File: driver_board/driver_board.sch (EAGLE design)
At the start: 18 parts, among them Q1 IRLML6346TRPBF, U1 AL5812MP-13

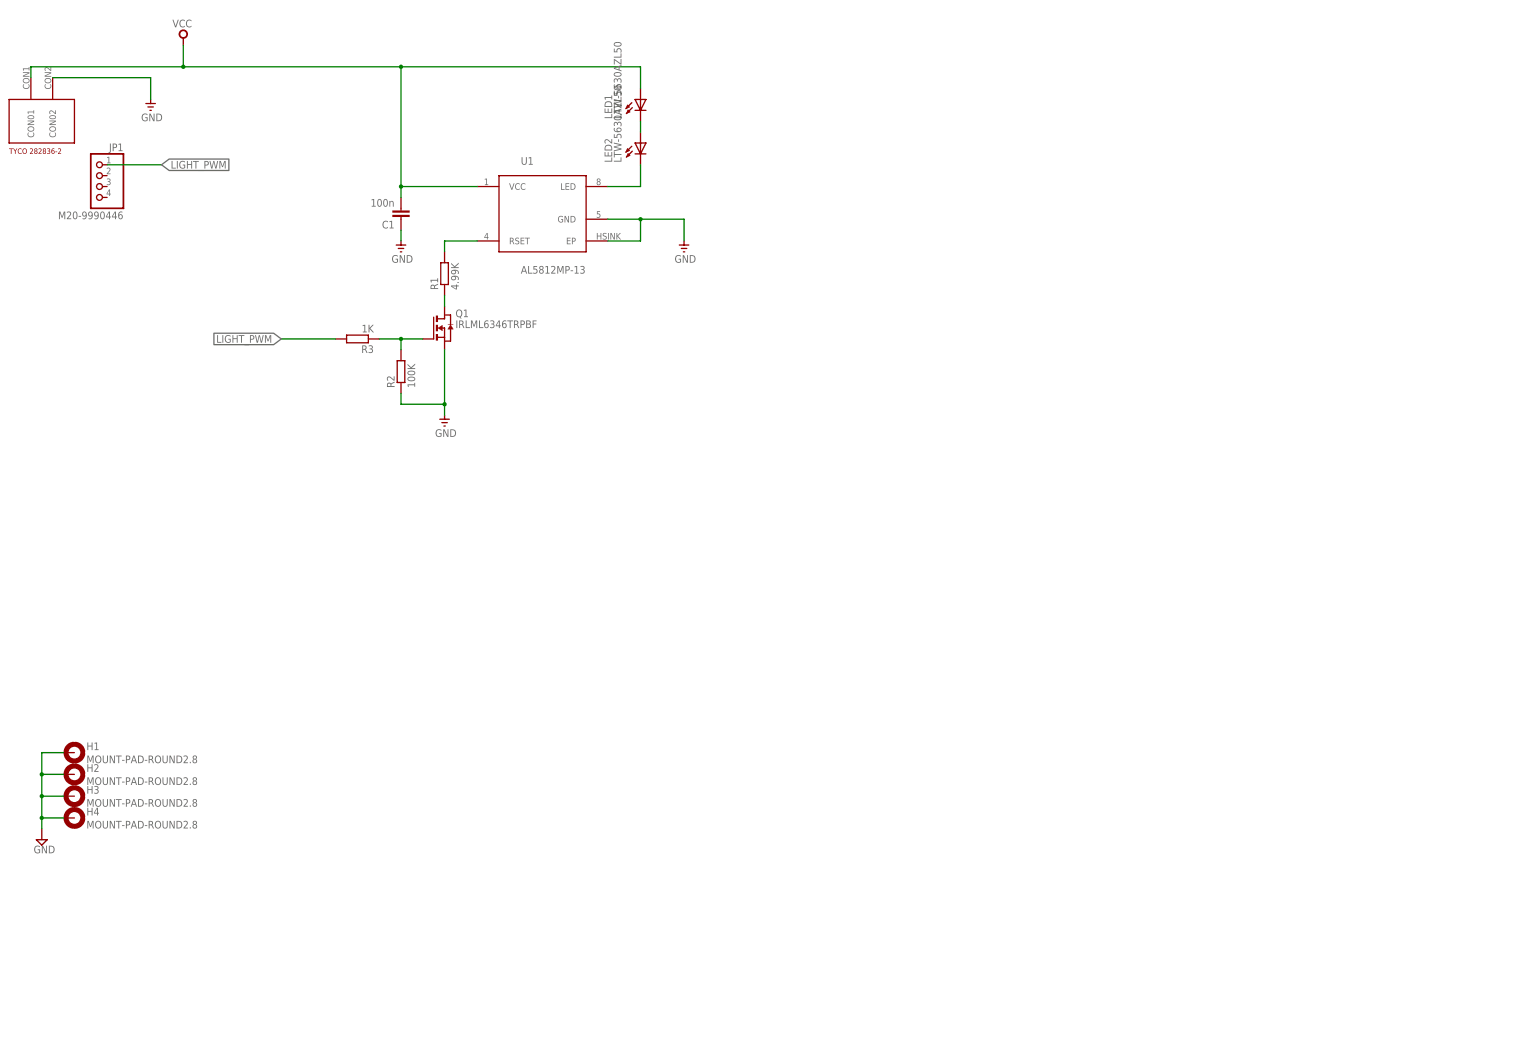
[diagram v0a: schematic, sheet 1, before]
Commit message: driver board 0.3 not completed
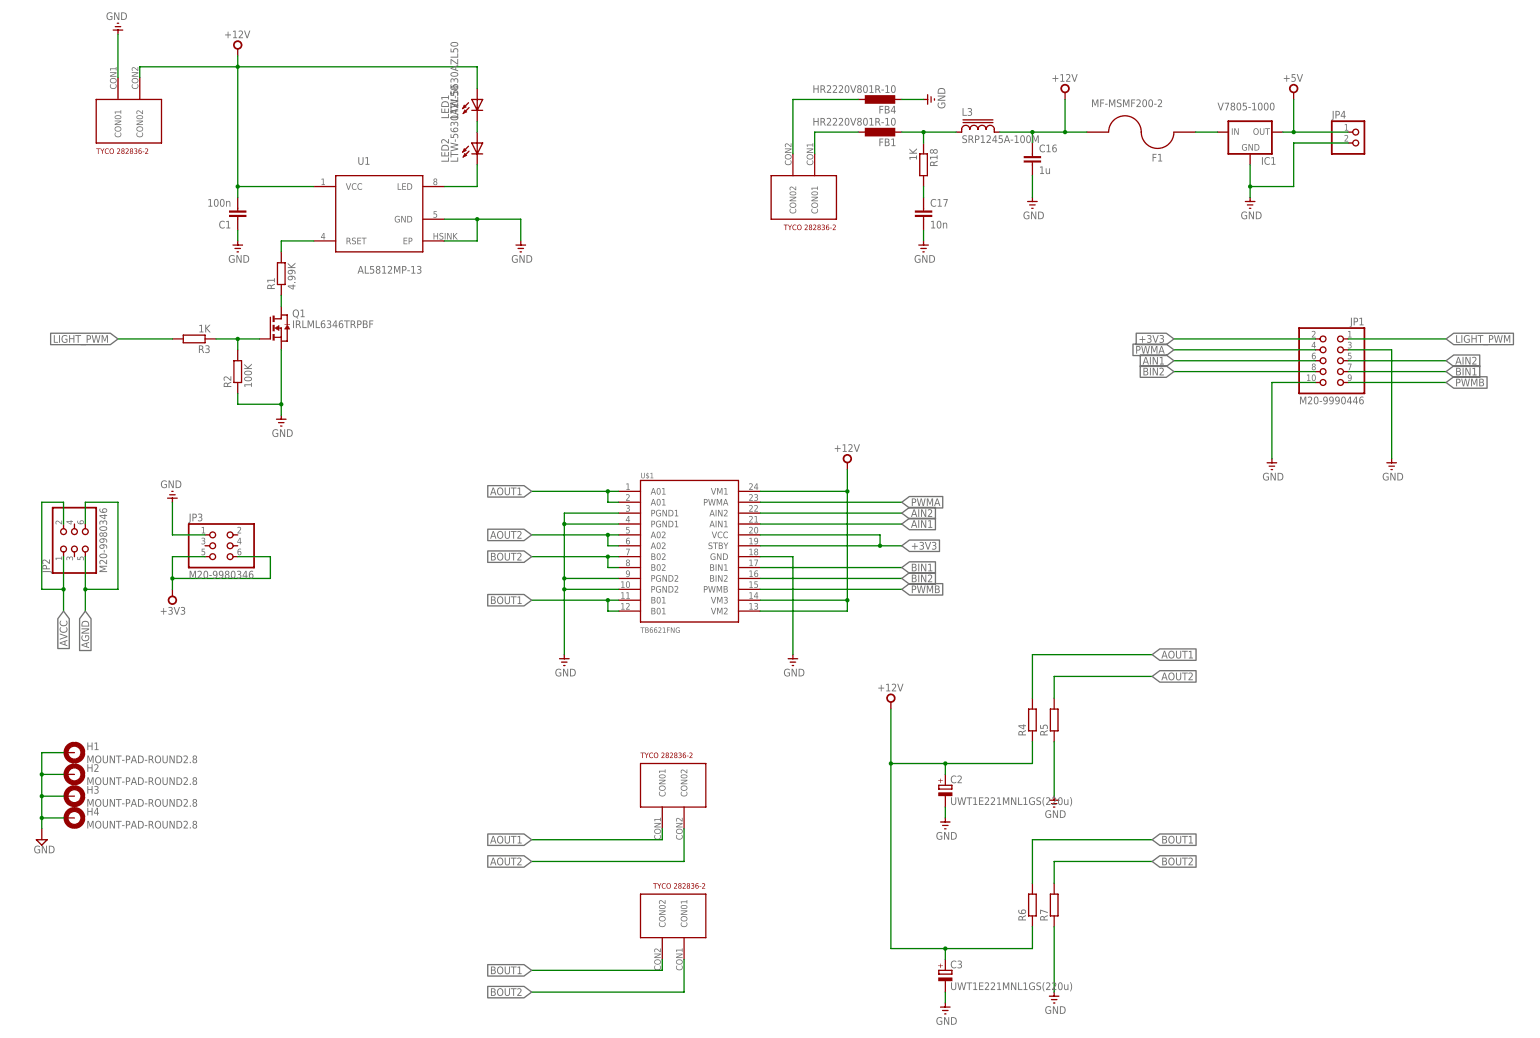
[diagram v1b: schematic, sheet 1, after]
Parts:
- removed ESC1, ESC2: ESC_POWER, openblw:ESC_POWER
- added C16: 1u, resistor:C-EUC0402
- added C17: 10n, resistor:C-EUC0402
- added F1: MF-MSMF200-2, openblw:MF-MSMF075/24
- added FB1, FB4: HR2220V801R-10, resistor:L-EUL5650M
- added IC1: V7805-1000, openblw:VR_1OUTXX
- added JP2, JP3: M20-9980346, pinhead:PINHD-2X3
- added JP4: (no value), pinhead:PINHD-1X2
- added L3: SRP1245A-100M, openblw:SRP1250A
- added R18: 1K, resistor:R-EU_R0402
- added R4, R5, R6, R7: (no value), resistor:R-EU_R0805
- added U$2, U$4, U$7, U$8: 282836-2, openblw:282836-2
- JP1: device pinhead:PINHD-1X4 -> pinhead:PINHD-2X5
- U$1: value 282836-2 -> TB6621FNG; device openblw:282836-2 -> openblw:TB6621FNG
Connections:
- removed net VCC: C1.2, C2.+, C3.+, ESC1.POWER, ESC2.POWER, LED1.A, U$1.CON01, U1.VCC
- new net +12V: C1.2, C16.1, C2.+, C3.+, F1.1, L3.2, LED1.A, R4.1, R6.1, U$1.VM1, U$1.VM2, U$1.VM3, U$4.CON02, U1.VCC
- new net +3V3: JP1.2, JP3.5, JP3.6, U$1.STBY, U$1.VCC
- new net +5V: IC1.OUT, JP4.1
- new net AGND: FB4.1, JP2.5, JP2.6, U$2.CON02
- new net AIN1: JP1.6, U$1.AIN1
- new net AIN2: JP1.5, U$1.AIN2
- new net AOUT1: R4.2, U$1.A01@1, U$1.A01@2, U$8.CON01
- new net AOUT2: R5.2, U$1.A02@5, U$1.A02@6, U$8.CON02
- new net AVCC: FB1.1, JP2.1, JP2.2, U$2.CON01
- new net BIN1: JP1.7, U$1.BIN1
- new net BIN2: JP1.8, U$1.BIN2
- new net BOUT1: R6.2, U$1.B01@11, U$1.B01@12, U$7.CON02
- new net BOUT2: R7.2, U$1.B02@7, U$1.B02@8, U$7.CON01
- new net N$3: FB1.2, L3.1, R18.1
- new net N$38: C17.1, R18.2
- new net N$39: F1.2, IC1.IN
- new net PWMA: JP1.4, U$1.PWMA
- new net PWMB: JP1.9, U$1.PWMB
- net GND: now also C16.2, C17.2, FB4.2, IC1.GND, JP1.10, JP1.3, JP3.1, JP4.2, R5.1, R7.1, U$1.GND, U$1.PGND1@3, U$1.PGND1@4, U$1.PGND2@10, U$1.PGND2@9, U$4.CON01; no longer ESC1.GND, ESC2.GND, U$1.CON02
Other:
- moved on the sheet: C1, LED1, LED2, Q1, R1, R2, R3, U1

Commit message: driver board 0.3
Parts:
- JP2, JP3: device pinhead:PINHD-2X3 -> pinhead+:PINHD-2X3SMT
- renumbered U$1 to U2
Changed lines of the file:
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@@
 <part name="L3" library="openblw" deviceset="SRP1250A" device="" value="SRP1245A-100M"/>
 <part name="FB4" library="resistor" deviceset="L-EU" device="L5650M" value="HR2220V801R-10"/>
-<part name="JP2" library="pinhead" deviceset="PINHD-2X3" device="" value="M20-9980346"/>
-<part name="JP3" library="pinhead" deviceset="PINHD-2X3" device="" value="M20-9980346"/>
+<part name="JP2" library="pinhead+" deviceset="PINHD-2X3" device="SMT" value="M20-9980346"/>
+<part name="JP3" library="pinhead+" deviceset="PINHD-2X3" device="SMT" value="M20-9980346"/>
 <part name="V7" library="supply" deviceset="+3V3" device=""/>
 <part name="GND11" library="supply" deviceset="GND" device=""/>
 <part name="V3" library="supply" deviceset="+12V" device=""/>
-<part name="U$1" library="openblw" deviceset="TB6621FNG" device=""/>
+<part name="U2" library="openblw" deviceset="TB6621FNG" device=""/>
 <part name="U$4" library="openblw" deviceset="282836-2" device=""/>
 <part name="GND4" library="supply" deviceset="GND" device=""/>
@@
 <instance part="R6" gate="G$1" x="248.92" y="35.56" rot="R90"/>
 <instance part="R7" gate="G$1" x="254" y="35.56" rot="R90"/>
-<instance part="U$1" gate="G$1" x="170.18" y="119.38"/>
+<instance part="U2" gate="G$1" x="170.18" y="119.38"/>
 <instance part="V4" gate="1" x="205.74" y="139.7"/>
 <instance part="GND10" gate="1" x="193.04" y="91.44"/>
@@
 </segment>
 <segment>
-<pinref part="U$1" gate="G$1" pin="PGND1@3"/>
+<pinref part="U2" gate="G$1" pin="PGND1@3"/>
 <wire x1="152.4" y1="127" x2="139.7" y2="127" width="0.1524" layer="91"/>
 <wire x1="139.7" y1="127" x2="139.7" y2="124.46" width="0.1524" layer="91"/>
-<pinref part="U$1" gate="G$1" pin="PGND1@4"/>
+<pinref part="U2" gate="G$1" pin="PGND1@4"/>
 <wire x1="139.7" y1="124.46" x2="139.7" y2="111.76" width="0.1524" layer="91"/>
 <wire x1="139.7" y1="111.76" x2="139.7" y2="109.22" width="0.1524" layer="91"/>
@@
 <wire x1="152.4" y1="124.46" x2="139.7" y2="124.46" width="0.1524" layer="91"/>
 <junction x="139.7" y="124.46"/>
-<pinref part="U$1" gate="G$1" pin="PGND2@9"/>
+<pinref part="U2" gate="G$1" pin="PGND2@9"/>
 <wire x1="152.4" y1="111.76" x2="139.7" y2="111.76" width="0.1524" layer="91"/>
 <junction x="139.7" y="111.76"/>
-<pinref part="U$1" gate="G$1" pin="PGND2@10"/>
+<pinref part="U2" gate="G$1" pin="PGND2@10"/>
 <wire x1="152.4" y1="109.22" x2="139.7" y2="109.22" width="0.1524" layer="91"/>
 <junction x="139.7" y="109.22"/>
@@
 </segment>
 <segment>
-<pinref part="U$1" gate="G$1" pin="GND"/>
+<pinref part="U2" gate="G$1" pin="GND"/>
 <wire x1="185.42" y1="116.84" x2="193.04" y2="116.84" width="0.1524" layer="91"/>
 <wire x1="193.04" y1="116.84" x2="193.04" y2="93.98" width="0.1524" layer="91"/>
@@
 </segment>
 <segment>
-<pinref part="U$1" gate="G$1" pin="VM1"/>
+<pinref part="U2" gate="G$1" pin="VM1"/>
 <pinref part="V4" gate="1" pin="+12V"/>
 <wire x1="185.42" y1="132.08" x2="205.74" y2="132.08" width="0.1524" layer="91"/>
 <wire x1="205.74" y1="132.08" x2="205.74" y2="137.16" width="0.1524" layer="91"/>
-<pinref part="U$1" gate="G$1" pin="VM3"/>
+<pinref part="U2" gate="G$1" pin="VM3"/>
 <wire x1="185.42" y1="106.68" x2="205.74" y2="106.68" width="0.1524" layer="91"/>
 <wire x1="205.74" y1="106.68" x2="205.74" y2="132.08" width="0.1524" layer="91"/>
 <junction x="205.74" y="132.08"/>
-<pinref part="U$1" gate="G$1" pin="VM2"/>
+<pinref part="U2" gate="G$1" pin="VM2"/>
 <wire x1="185.42" y1="104.14" x2="205.74" y2="104.14" width="0.1524" layer="91"/>
 <wire x1="205.74" y1="104.14" x2="205.74" y2="106.68" width="0.1524" layer="91"/>
@@
 </segment>
 <segment>
-<pinref part="U$1" gate="G$1" pin="STBY"/>
+<pinref part="U2" gate="G$1" pin="STBY"/>
 <wire x1="185.42" y1="119.38" x2="213.36" y2="119.38" width="0.1524" layer="91"/>
 <label x="218.44" y="119.38" size="1.778" layer="95" xref="yes"/>
-<pinref part="U$1" gate="G$1" pin="VCC"/>
+<pinref part="U2" gate="G$1" pin="VCC"/>
 <wire x1="213.36" y1="119.38" x2="218.44" y2="119.38" width="0.1524" layer="91"/>
 <wire x1="185.42" y1="121.92" x2="213.36" y2="121.92" width="0.1524" layer="91"/>
@@
 </segment>
 <segment>
-<pinref part="U$1" gate="G$1" pin="A01@1"/>
+<pinref part="U2" gate="G$1" pin="A01@1"/>
 <wire x1="152.4" y1="132.08" x2="149.86" y2="132.08" width="0.1524" layer="91"/>
-<pinref part="U$1" gate="G$1" pin="A01@2"/>
+<pinref part="U2" gate="G$1" pin="A01@2"/>
 <wire x1="149.86" y1="132.08" x2="132.08" y2="132.08" width="0.1524" layer="91"/>
 <wire x1="152.4" y1="129.54" x2="149.86" y2="129.54" width="0.1524" layer="91"/>
@@
 </segment>
 <segment>
-<pinref part="U$1" gate="G$1" pin="A02@5"/>
+<pinref part="U2" gate="G$1" pin="A02@5"/>
 <wire x1="152.4" y1="121.92" x2="149.86" y2="121.92" width="0.1524" layer="91"/>
-<pinref part="U$1" gate="G$1" pin="A02@6"/>
+<pinref part="U2" gate="G$1" pin="A02@6"/>
 <wire x1="149.86" y1="121.92" x2="132.08" y2="121.92" width="0.1524" layer="91"/>
 <wire x1="152.4" y1="119.38" x2="149.86" y2="119.38" width="0.1524" layer="91"/>
@@
 </segment>
 <segment>
-<pinref part="U$1" gate="G$1" pin="B02@7"/>
+<pinref part="U2" gate="G$1" pin="B02@7"/>
 <wire x1="152.4" y1="116.84" x2="149.86" y2="116.84" width="0.1524" layer="91"/>
-<pinref part="U$1" gate="G$1" pin="B02@8"/>
+<pinref part="U2" gate="G$1" pin="B02@8"/>
 <wire x1="149.86" y1="116.84" x2="132.08" y2="116.84" width="0.1524" layer="91"/>
 <wire x1="152.4" y1="114.3" x2="149.86" y2="114.3" width="0.1524" layer="91"/>
@@
 </segment>
 <segment>
-<pinref part="U$1" gate="G$1" pin="B01@11"/>
+<pinref part="U2" gate="G$1" pin="B01@11"/>
 <wire x1="152.4" y1="106.68" x2="149.86" y2="106.68" width="0.1524" layer="91"/>
-<pinref part="U$1" gate="G$1" pin="B01@12"/>
+<pinref part="U2" gate="G$1" pin="B01@12"/>
 <wire x1="149.86" y1="106.68" x2="132.08" y2="106.68" width="0.1524" layer="91"/>
 <wire x1="152.4" y1="104.14" x2="149.86" y2="104.14" width="0.1524" layer="91"/>
@@
 <net name="PWMA" class="0">
 <segment>
-<pinref part="U$1" gate="G$1" pin="PWMA"/>
+<pinref part="U2" gate="G$1" pin="PWMA"/>
 <wire x1="185.42" y1="129.54" x2="218.44" y2="129.54" width="0.1524" layer="91"/>
 <label x="218.44" y="129.54" size="1.778" layer="95" xref="yes"/>
@@
 <net name="AIN2" class="0">
 <segment>
-<pinref part="U$1" gate="G$1" pin="AIN2"/>
+<pinref part="U2" gate="G$1" pin="AIN2"/>
 <wire x1="185.42" y1="127" x2="218.44" y2="127" width="0.1524" layer="91"/>
 <label x="218.44" y="127" size="1.778" layer="95" xref="yes"/>
@@
 <net name="AIN1" class="0">
 <segment>
-<pinref part="U$1" gate="G$1" pin="AIN1"/>
+<pinref part="U2" gate="G$1" pin="AIN1"/>
 <wire x1="185.42" y1="124.46" x2="218.44" y2="124.46" width="0.1524" layer="91"/>
 <label x="218.44" y="124.46" size="1.778" layer="95" xref="yes"/>
@@
 <net name="BIN1" class="0">
 <segment>
-<pinref part="U$1" gate="G$1" pin="BIN1"/>
+<pinref part="U2" gate="G$1" pin="BIN1"/>
 <wire x1="185.42" y1="114.3" x2="218.44" y2="114.3" width="0.1524" layer="91"/>
 <label x="218.44" y="114.3" size="1.778" layer="95" xref="yes"/>
@@
 <net name="BIN2" class="0">
 <segment>
-<pinref part="U$1" gate="G$1" pin="BIN2"/>
+<pinref part="U2" gate="G$1" pin="BIN2"/>
 <wire x1="185.42" y1="111.76" x2="218.44" y2="111.76" width="0.1524" layer="91"/>
 <label x="218.44" y="111.76" size="1.778" layer="95" xref="yes"/>
@@
 <net name="PWMB" class="0">
 <segment>
-<pinref part="U$1" gate="G$1" pin="PWMB"/>
+<pinref part="U2" gate="G$1" pin="PWMB"/>
 <wire x1="185.42" y1="109.22" x2="218.44" y2="109.22" width="0.1524" layer="91"/>
 <label x="218.44" y="109.22" size="1.778" layer="95" xref="yes"/>
